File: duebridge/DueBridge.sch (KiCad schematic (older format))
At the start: 36 parts, among them IC1 4N35, IC2 4N35, K1 1Wire, P1 Wind Sensor, P2 Water Sensor, P3 CAN0, P4 CAN1, P5 I2C, U1 DCDC, U2 SDCard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

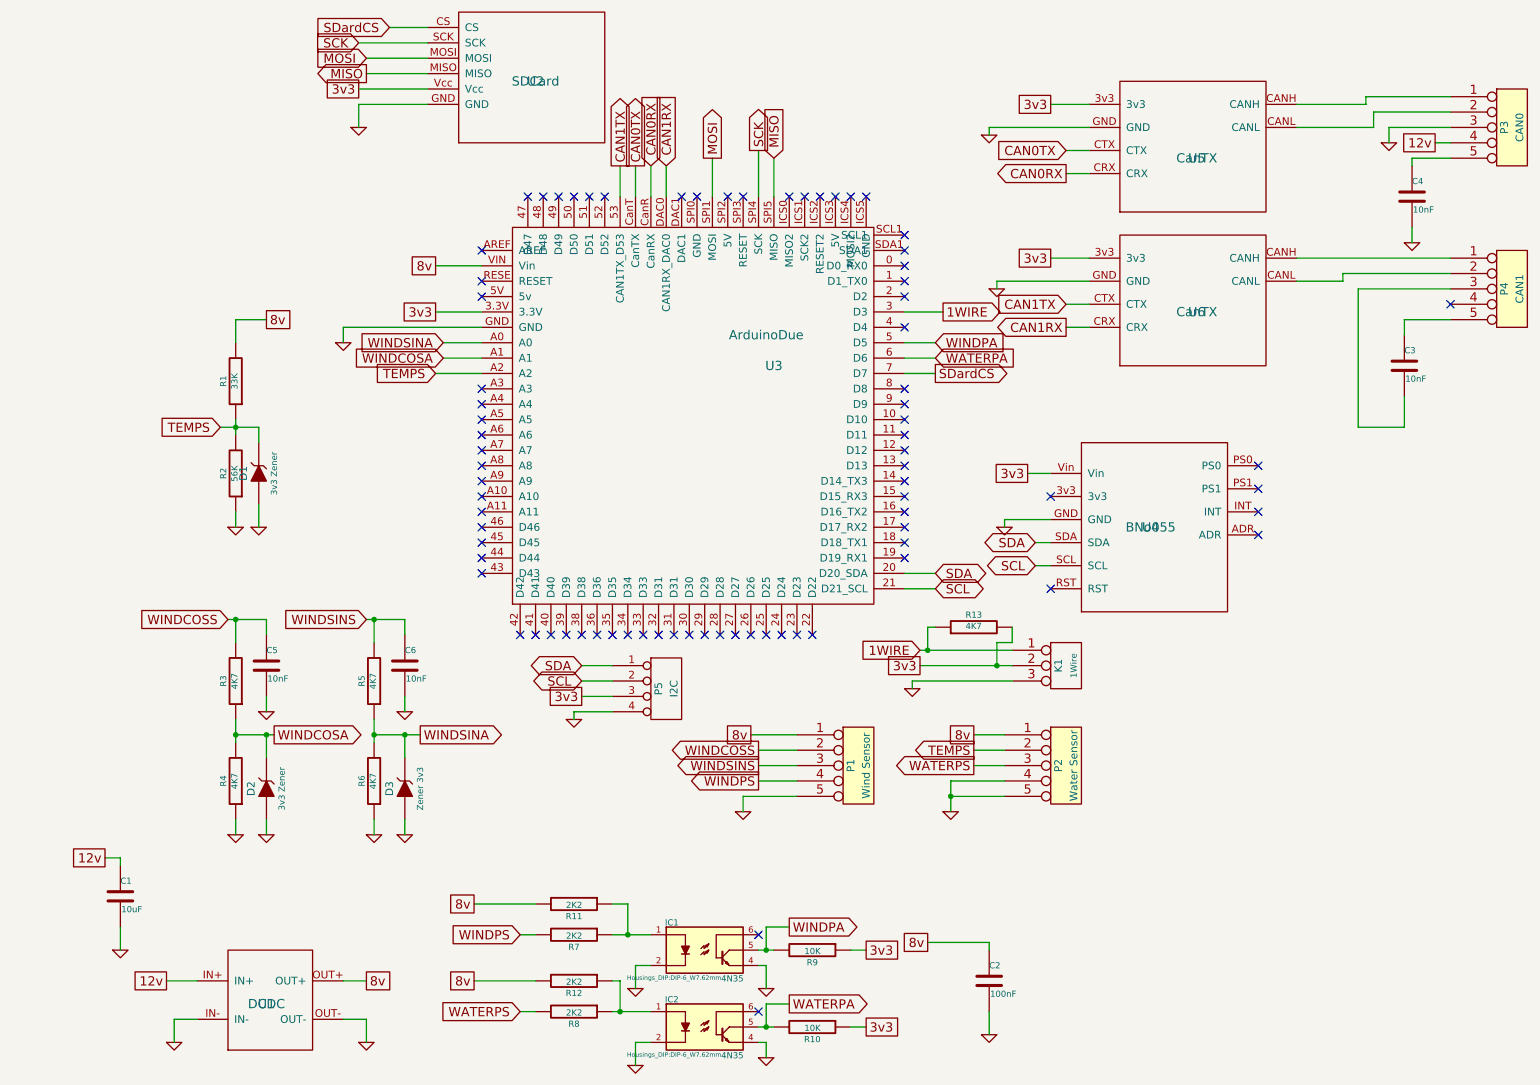
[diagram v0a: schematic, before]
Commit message: Tested pulse sensors, and basic PGN output.
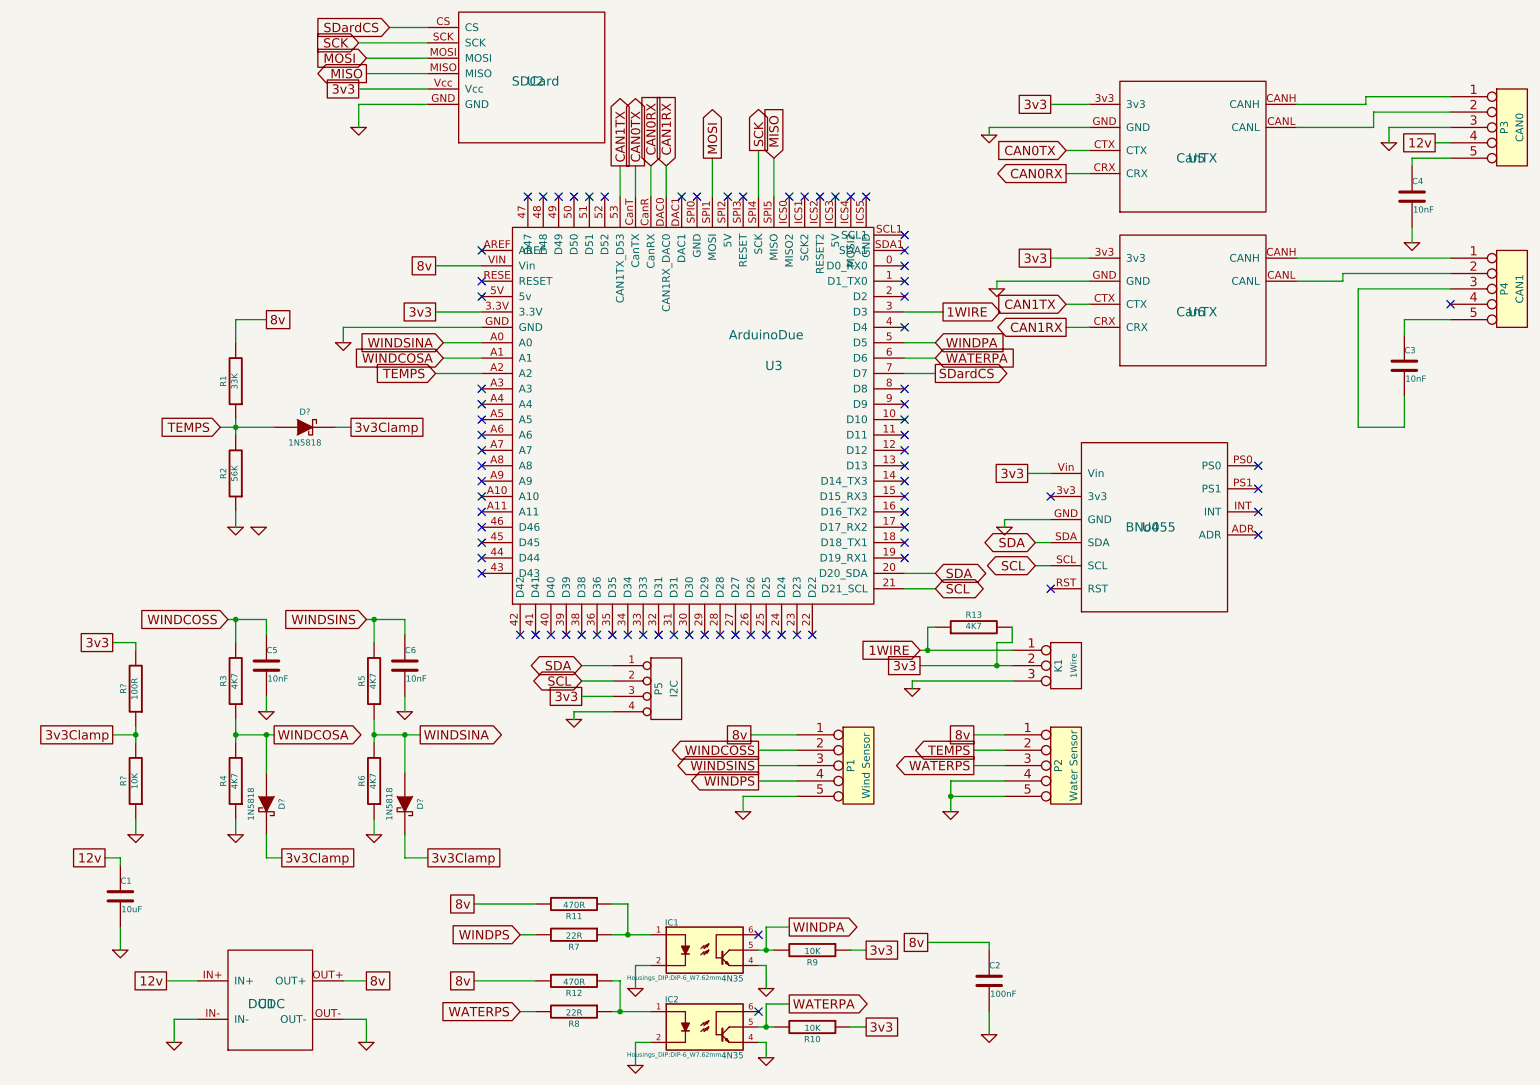
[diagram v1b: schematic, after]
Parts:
- removed D1, D2: 3v3 Zener, Resistors_ThroughHole:Resistor_Horizontal_RM7mm, symbol ZENER
- removed D3: Zener 3v3, Resistors_ThroughHole:Resistor_Horizontal_RM7mm, symbol ZENER
- added D? (x3): 1N5818, symbol DIODESCH
- added R?: 10K, Resistors_ThroughHole:Resistor_Horizontal_RM7mm, symbol R
- added R?: 100R, Resistors_ThroughHole:Resistor_Horizontal_RM7mm, symbol R
- R11, R12: value 2K2 -> 470R
- R7, R8: value 2K2 -> 22R
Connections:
- net 3v3: now also R?.2
- net GND: now also R?.1
- net TEMPS: now also D?.1 (A)
- net WINDCOSA: now also D?.1 (A)
- net WINDSINA: now also D?.1 (A)
- new net 3v3Clamp: D?.2 (K), D?.2 (K), D?.2 (K), R?.1, R?.2
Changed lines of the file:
@@
 LIBS:instruments
 LIBS:customparts
+LIBS:DueBridge-cache
 EELAYER 25 0
 EELAYER END
@@
 P 3800 6650
 F 0 "R7" V 3880 6650 40  0000 C CNN
-F 1 "2K2" V 3807 6651 40  0000 C CNN
+F 1 "22R" V 3807 6651 40  0000 C CNN
 F 2 "Resistors_ThroughHole:Resistor_Horizontal_RM7mm" V 3730 6650 30  0001 C CNN
 F 3 "" H 3800 6650 30  0000 C CNN
@@
 P 3800 7150
 F 0 "R8" V 3880 7150 40  0000 C CNN
-F 1 "2K2" V 3807 7151 40  0000 C CNN
+F 1 "22R" V 3807 7151 40  0000 C CNN
 F 2 "Resistors_ThroughHole:Resistor_Horizontal_RM7mm" V 3730 7150 30  0001 C CNN
 F 3 "" H 3800 7150 30  0000 C CNN
@@
 $EndComp
 $Comp
-L ZENER D2
-U 1 1 5A0E00C3
-P 1800 5700
-F 0 "D2" H 1800 5800 50  0000 C CNN
-F 1 "3v3 Zener" H 1800 5600 40  0000 C CNN
-F 2 "Resistors_ThroughHole:Resistor_Horizontal_RM7mm" H 1800 5700 60  0001 C CNN
-F 3 "" H 1800 5700 60  0000 C CNN
-	1    1800 5700
-	0    -1   -1   0
-$EndComp
-$Comp
 L GND #PWR012
 U 1 1 5A0E01A2
@@
 F 3 "" H 1600 6000 60  0001 C CNN
 	1    1600 6000
-	1    0    0    -1
-$EndComp
-$Comp
-L GND #PWR013
-U 1 1 5A0E01DA
-P 1800 6000
-F 0 "#PWR013" H 1800 6000 30  0001 C CNN
-F 1 "GND" H 1800 5930 30  0001 C CNN
-F 2 "" H 1800 6000 60  0001 C CNN
-F 3 "" H 1800 6000 60  0001 C CNN
-	1    1800 6000
 	1    0    0    -1
 $EndComp
@@
 $EndComp
 $Comp
-L ZENER D3
-U 1 1 5A0E03D2
-P 2700 5700
-F 0 "D3" H 2700 5800 50  0000 C CNN
-F 1 "Zener 3v3" H 2700 5600 40  0000 C CNN
-F 2 "Resistors_ThroughHole:Resistor_Horizontal_RM7mm" H 2700 5700 60  0001 C CNN
-F 3 "" H 2700 5700 60  0000 C CNN
-	1    2700 5700
-	0    -1   -1   0
-$EndComp
-$Comp
 L GND #PWR014
 U 1 1 5A0E03DB
@@
 F 3 "" H 2500 6000 60  0001 C CNN
 	1    2500 6000
-	1    0    0    -1
-$EndComp
-$Comp
-L GND #PWR015
-U 1 1 5A0E03E1
-P 2700 6000
-F 0 "#PWR015" H 2700 6000 30  0001 C CNN
-F 1 "GND" H 2700 5930 30  0001 C CNN
-F 2 "" H 2700 6000 60  0001 C CNN
-F 3 "" H 2700 6000 60  0001 C CNN
-	1    2700 6000
 	1    0    0    -1
 $EndComp
@@
 Text GLabel 2900 3000 0    60   Input ~ 0
 TEMPS
-$Comp
-L ZENER D1
-U 1 1 5A0E1FF8
-P 1750 3650
-F 0 "D1" H 1750 3750 50  0000 C CNN
-F 1 "3v3 Zener" H 1750 3550 40  0000 C CNN
-F 2 "Resistors_ThroughHole:Resistor_Horizontal_RM7mm" H 1750 3650 60  0001 C CNN
-F 3 "" H 1750 3650 60  0000 C CNN
-	1    1750 3650
-	0    -1   -1   0
-$EndComp
 $Comp
 L GND #PWR017
@@
 P 3800 6450
 F 0 "R11" V 3880 6450 40  0000 C CNN
-F 1 "2K2" V 3807 6451 40  0000 C CNN
+F 1 "470R" V 3807 6451 40  0000 C CNN
 F 2 "Resistors_ThroughHole:Resistor_Horizontal_RM7mm" V 3730 6450 30  0001 C CNN
 F 3 "" H 3800 6450 30  0000 C CNN
@@
 P 3800 6950
 F 0 "R12" V 3880 6950 40  0000 C CNN
-F 1 "2K2" V 3807 6951 40  0000 C CNN
+F 1 "470R" V 3807 6951 40  0000 C CNN
 F 2 "Resistors_ThroughHole:Resistor_Horizontal_RM7mm" V 3730 6950 30  0001 C CNN
 F 3 "" H 3800 6950 30  0000 C CNN
@@
 	1600 5250 1600 5400
 Wire Wire Line
-	1800 5500 1800 5350
+	1800 5350 1800 5600
 Wire Wire Line
 	1600 5350 1850 5350
 Connection ~ 1600 5350
 Wire Wire Line
-	1800 5900 1800 6000
-Wire Wire Line
 	1600 5900 1600 6000
 Wire Wire Line
@@
 	2500 5250 2500 5400
 Wire Wire Line
-	2700 5500 2700 5350
+	2700 5350 2700 5600
 Wire Wire Line
 	2500 5350 2800 5350
 Connection ~ 2500 5350
-Wire Wire Line
-	2700 5900 2700 6000
 Wire Wire Line
 	2500 5900 2500 6000
@@
 	1600 4000 1600 3900
 Wire Wire Line
-	1500 3350 1750 3350
+	1500 3350 1850 3350
 Connection ~ 1600 3350
 Wire Wire Line
 	2900 3000 3200 3000
-Wire Wire Line
-	1750 3350 1750 3450
-Wire Wire Line
-	1750 3850 1750 4000
 Wire Wire Line
 	6150 2800 5950 2800
@@
 	6000 5000 6000 5050
 Wire Wire Line
-	6650 4900 6050 4900
-Wire Wire Line
-	6650 4800 6050 4800
+	6050 4900 6650 4900
+Wire Wire Line
+	6050 4800 6650 4800
 $Comp
 L R R13
@@
 Wire Wire Line
 	4050 4900 3850 4900
+$Comp
+L DIODESCH D?
+U 1 1 5A2ABF2F
+P 2050 3350
+F 0 "D?" H 2050 3450 40  0000 C CNN
+F 1 "1N5818" H 2050 3250 40  0000 C CNN
+F 2 "" H 2050 3350 60  0000 C CNN
+F 3 "" H 2050 3350 60  0000 C CNN
+	1    2050 3350
+	1    0    0    -1
+$EndComp
+$Comp
+L R R?
+U 1 1 5A2AC170
+P 950 5650
+F 0 "R?" V 1030 5650 40  0000 C CNN
+F 1 "10K" V 957 5651 40  0000 C CNN
+F 2 "Resistors_ThroughHole:Resistor_Horizontal_RM7mm" V 880 5650 30  0001 C CNN
+F 3 "" H 950 5650 30  0000 C CNN
+	1    950  5650
+	-1   0    0    1
+$EndComp
+$Comp
+L R R?
+U 1 1 5A2AC206
+P 950 5050
+F 0 "R?" V 1030 5050 40  0000 C CNN
+F 1 "100R" V 957 5051 40  0000 C CNN
+F 2 "Resistors_ThroughHole:Resistor_Horizontal_RM7mm" V 880 5050 30  0001 C CNN
+F 3 "" H 950 5050 30  0000 C CNN
+	1    950  5050
+	-1   0    0    1
+$EndComp
+Text GLabel 800  4750 0    60   UnSpc ~ 0
+3v3
+Text GLabel 800  5350 0    60   UnSpc ~ 0
+3v3Clamp
+$Comp
+L GND #PWR?
+U 1 1 5A2AC461
+P 950 6000
+F 0 "#PWR?" H 950 6000 30  0001 C CNN
+F 1 "GND" H 950 5930 30  0001 C CNN
+F 2 "" H 950 6000 60  0001 C CNN
+F 3 "" H 950 6000 60  0001 C CNN
+	1    950  6000
+	1    0    0    -1
+$EndComp
+Wire Wire Line
+	950  6000 950  5900
+Wire Wire Line
+	950  5300 950  5400
+Wire Wire Line
+	800  5350 950  5350
+Connection ~ 950  5350
+Wire Wire Line
+	800  4750 950  4750
+Wire Wire Line
+	950  4750 950  4800
+Text GLabel 2350 3350 2    60   UnSpc ~ 0
+3v3Clamp
+Wire Wire Line
+	2250 3350 2350 3350
+$Comp
+L DIODESCH D?
+U 1 1 5A2AD0D8
+P 1800 5800
+F 0 "D?" H 1800 5900 40  0000 C CNN
+F 1 "1N5818" H 1800 5700 40  0000 C CNN
+F 2 "" H 1800 5800 60  0000 C CNN
+F 3 "" H 1800 5800 60  0000 C CNN
+	1    1800 5800
+	0    1    1    0
+$EndComp
+$Comp
+L DIODESCH D?
+U 1 1 5A2AD18B
+P 2700 5800
+F 0 "D?" H 2700 5900 40  0000 C CNN
+F 1 "1N5818" H 2700 5700 40  0000 C CNN
+F 2 "" H 2700 5800 60  0000 C CNN
+F 3 "" H 2700 5800 60  0000 C CNN
+	1    2700 5800
+	0    1    1    0
+$EndComp
+Text GLabel 1900 6150 2    60   UnSpc ~ 0
+3v3Clamp
+Text GLabel 2850 6150 2    60   UnSpc ~ 0
+3v3Clamp
+Wire Wire Line
+	2700 6000 2700 6150
+Wire Wire Line
+	2700 6150 2850 6150
+Wire Wire Line
+	1900 6150 1800 6150
+Wire Wire Line
+	1800 6150 1800 6000
 $EndSCHEMATC
